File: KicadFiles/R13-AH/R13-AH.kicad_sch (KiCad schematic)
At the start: 30 parts, among them J1 Conn_01x01_Pin, J2 Conn_01x04_MountingPin, J3 Conn_01x04_MountingPin, SW1 SW_DPST_x2, SW2 SW_DPST_x2, U1 TPD4E05U06DQAR, U2 STM32F072CBTx, U3 XC6206PxxxMR

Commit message: Add and update KiCad design assets for R12/R13 variants
- refresh existing R12-AW, R13-AH, and R13-BW project files
- add the R13-AW project and variant-specific placer configs
- add 12u/13u outlines and normalize layout JSON filenames
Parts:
- removed H1: MountingHole_Pad, My-Fi Footprints:Cherry-GND-PAD, symbol Mechanical:MountingHole_Pad
- added D1, D10, D11, D12, D14, D15, D16, D17, D18, D19, D2, D20, D21, D22, D23, D24, D25, D26, D27, D28, D29, D3, D30, D31, D32, D33, D34, D35, D36, D38, D39, D4, D41, D42, D43, D44, D45, D46, D47, D48, D49, D5, D50, D6, D7, D8, D9: 1N4148WS, My-Fi Footprints:D_SOD-323_HandSoldering, symbol Device:D
- added MX1, MX10, MX11, MX12, MX13, MX14, MX16, MX17, MX18, MX19, MX2, MX20, MX21, MX22, MX23, MX24, MX25, MX28, MX29, MX3, MX30, MX31, MX32, MX33, MX34, MX35, MX36, MX37, MX39, MX4, MX41, MX42, MX45, MX46, MX47, MX5, MX50, MX6, MX7, MX8, MX9: MX_SW_solder, My-Fi Footprints:SW_MX_1u, symbol PCM_marbastlib-mx:MX_SW_solder
- added MX15, MX38, MX40, MX43, MX48, MX49: MX_SW_solder, My-Fi Footprints:SW_MX_1.25u, symbol PCM_marbastlib-mx:MX_SW_solder
- added MX26, MX27, MX44: MX_SW_solder, My-Fi Footprints:SW_MX_1.75u, symbol PCM_marbastlib-mx:MX_SW_solder
- added S13, S47: MX_stab, My-Fi Footprints:STAB_MX_2u, symbol PCM_marbastlib-mx:MX_stab
- added S39: MX_stab, My-Fi Footprints:STAB_MX_2.25u, symbol PCM_marbastlib-mx:MX_stab
- added S46: MX_stab, My-Fi Footprints:STAB_MX_6.25u, symbol PCM_marbastlib-mx:MX_stab
- C1, C2, C3, C4, C5, C6, C7, C8, C9: footprint Capacitor_SMD:C_0805_2012Metric_Pad1.18x1.45mm_HandSolder -> Capacitor_SMD:C_0402_1005Metric
- LED2: footprint My-Fi Footprints:CAPS_LED_MX_3mm -> My-Fi Footprints:DIP_LED_MX_3mm
- R1, R2, R3, R4, R5, R6: footprint Resistor_SMD:R_0805_2012Metric_Pad1.20x1.40mm_HandSolder -> Resistor_SMD:R_0402_1005Metric
- renumbered D1 to D201
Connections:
- net +5V: no longer J2.1 (Pin_1)
- net VBUS: now also J2.1 (Pin_1)
- new net: D22.2 (A), MX22.2
- new net: D42.2 (A), MX42.2
- new net: D14.2 (A), MX13.2, MX14.2
- new net: D20.2 (A), MX20.2
- new net: D31.2 (A), MX31.2
- new net: D24.2 (A), MX24.2
- new net: D6.2 (A), MX6.2
- new net: D16.2 (A), MX16.2
- new net: D15.2 (A), MX15.2
- new net: D5.2 (A), MX5.2
- new net: D27.2 (A), MX27.2
- new net: D38.2 (A), MX37.2, MX38.2
- new net: D19.2 (A), MX19.2
- new net: D18.2 (A), MX18.2
- new net: D8.2 (A), MX8.2
- new net: D11.2 (A), MX11.2
- new net: D49.2 (A), MX49.2
- new net: D39.2 (A), MX39.2
- new net: D21.2 (A), MX21.2
- new net: D44.2 (A), MX44.2
- new net: D36.2 (A), MX36.2
- new net: D17.2 (A), MX17.2
- new net: D23.2 (A), MX23.2
- new net: D28.2 (A), MX28.2
- new net: D4.2 (A), MX4.2
- new net: D12.2 (A), MX12.2
- new net: D43.2 (A), MX43.2
- new net: D47.2 (A), MX47.2
- new net: D41.2 (A), MX40.2, MX41.2
- new net: D10.2 (A), MX10.2
- new net: D3.2 (A), MX3.2
- new net: D34.2 (A), MX34.2
- new net: D50.2 (A), MX50.2
- new net: D2.2 (A), MX2.2
- new net: D30.2 (A), MX30.2
- new net: D29.2 (A), MX29.2
- new net: D48.2 (A), MX48.2
- new net: D26.2 (A), MX26.2
- new net: D7.2 (A), MX7.2
- new net: D25.2 (A), MX25.2
- new net: D9.2 (A), MX9.2
- new net: D33.2 (A), MX33.2
- new net: D32.2 (A), MX32.2
- new net: D46.2 (A), MX46.2
- new net: D35.2 (A), MX35.2
- new net: D1.2 (A), MX1.2
- new net: D45.2 (A), MX45.2
- new net Col0: MX1.1, MX15.1, MX27.1
- new net Col1: MX16.1, MX2.1, MX28.1, MX42.1
- new net Col10: MX11.1, MX25.1, MX37.1, MX38.1, MX50.1
- new net Col11: MX12.1, MX39.1
- new net Col12: MX13.1, MX14.1, MX26.1, MX40.1, MX41.1
- new net Col2: MX17.1, MX29.1, MX3.1, MX43.1
- new net Col3: MX18.1, MX30.1, MX4.1, MX44.1
- new net Col4: MX19.1, MX31.1, MX45.1, MX5.1
- new net Col5: MX20.1, MX32.1, MX46.1, MX6.1
- new net Col6: MX21.1, MX33.1, MX47.1, MX7.1
- new net Col7: MX22.1, MX34.1, MX8.1
- new net Col8: MX23.1, MX35.1, MX48.1, MX9.1
- new net Col9: MX10.1, MX24.1, MX36.1, MX49.1
- new net Row0: D1.1 (K), D10.1 (K), D11.1 (K), D12.1 (K), D14.1 (K), D2.1 (K), D3.1 (K), D4.1 (K), D5.1 (K), D6.1 (K), D7.1 (K), D8.1 (K), D9.1 (K)
- new net Row1: D15.1 (K), D16.1 (K), D17.1 (K), D18.1 (K), D19.1 (K), D20.1 (K), D21.1 (K), D22.1 (K), D23.1 (K), D24.1 (K), D25.1 (K), D26.1 (K)
- new net Row2: D27.1 (K), D28.1 (K), D29.1 (K), D30.1 (K), D31.1 (K), D32.1 (K), D33.1 (K), D34.1 (K), D35.1 (K), D36.1 (K), D38.1 (K), D39.1 (K), D41.1 (K)
- new net Row3: D42.1 (K), D43.1 (K), D44.1 (K), D45.1 (K), D46.1 (K), D47.1 (K), D48.1 (K), D49.1 (K), D50.1 (K)
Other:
- moved on the sheet: C1, C2, C3, C4, C5, C6, C7, C8, C9, D201, F1, J1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

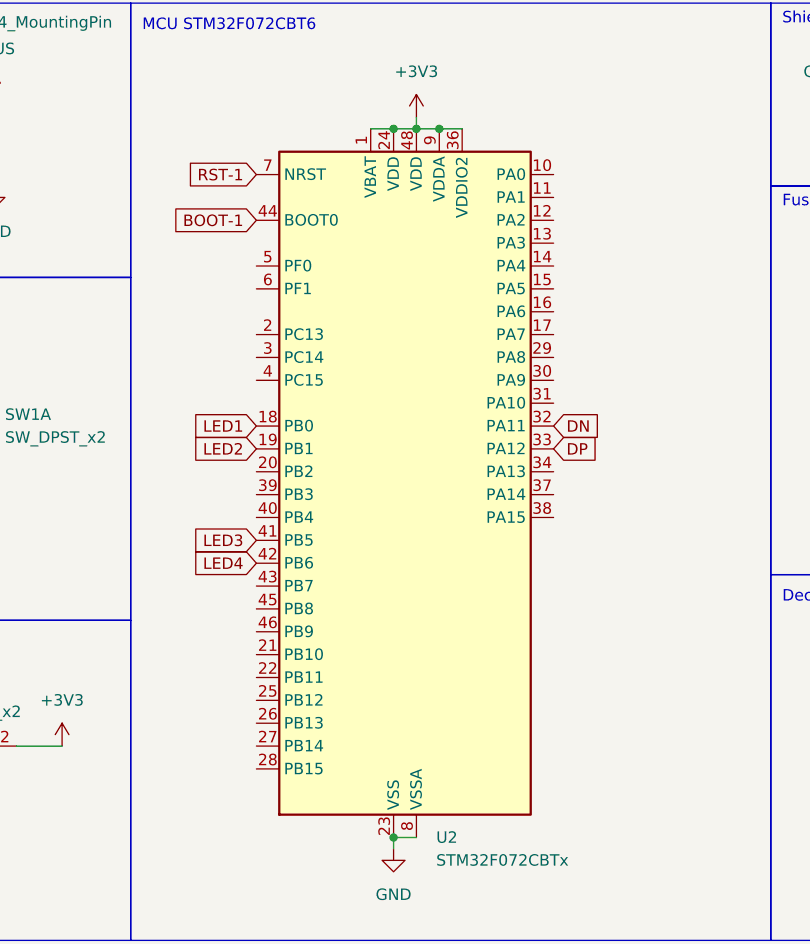
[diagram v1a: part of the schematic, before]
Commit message: Add global labels for columns and rows in R13-AH schematic
- Introduced new global labels for columns (Col0 to Col12) and rows (Row0 to Row3) in the R13-AH schematic.
- Each label includes properties for intersheet references, font size, justification, and positioning.
- Enhanced organization and readability of the schematic by clearly defining input and output connections.
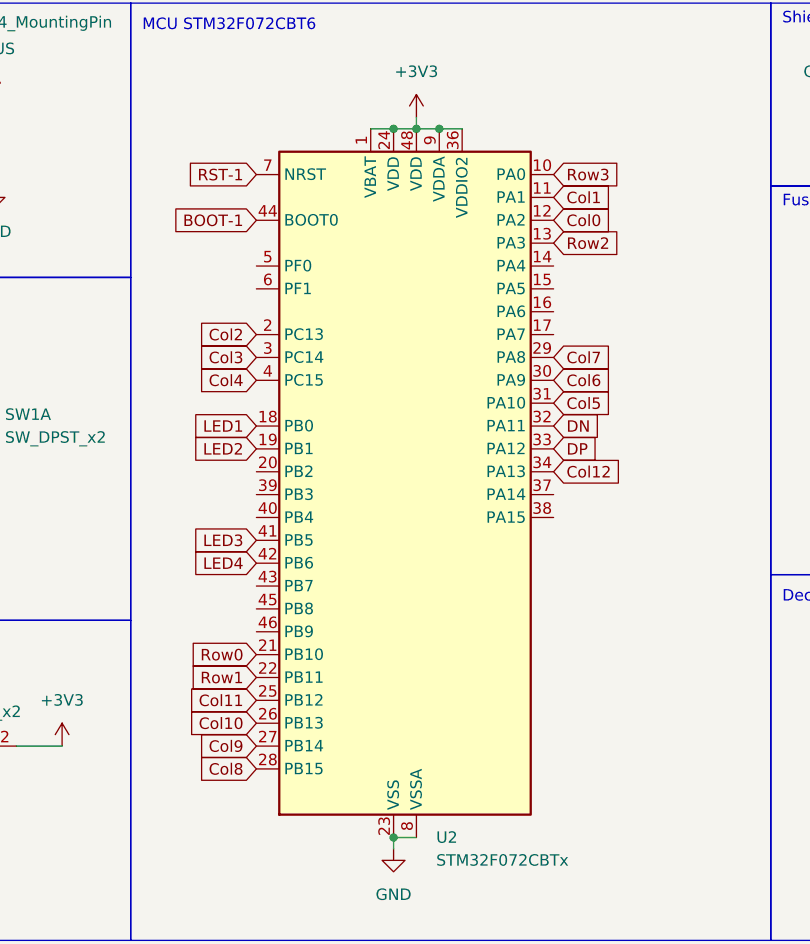
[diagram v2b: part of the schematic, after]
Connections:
- net Col0: now also U2.12 (PA2)
- net Col1: now also U2.11 (PA1)
- net Col10: now also U2.26 (PB13)
- net Col11: now also U2.25 (PB12)
- net Col12: now also U2.34 (PA13)
- net Col2: now also U2.2 (PC13)
- net Col3: now also U2.3 (PC14)
- net Col4: now also U2.4 (PC15)
- net Col5: now also U2.31 (PA10)
- net Col6: now also U2.30 (PA9)
- net Col7: now also U2.29 (PA8)
- net Col8: now also U2.28 (PB15)
- net Col9: now also U2.27 (PB14)
- net Row0: now also U2.21 (PB10)
- net Row1: now also U2.22 (PB11)
- net Row2: now also U2.13 (PA3)
- net Row3: now also U2.10 (PA0)
